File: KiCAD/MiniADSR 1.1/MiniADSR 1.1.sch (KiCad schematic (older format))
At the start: 35 parts, among them J1 INPUT, J2 OUTPUT, J4 ControlBoard_Pins, J6 MainBoard_Pins, Q1 BC547, Q2 BC547, Q3 BC547, U1 LM555xN, U2 TL072

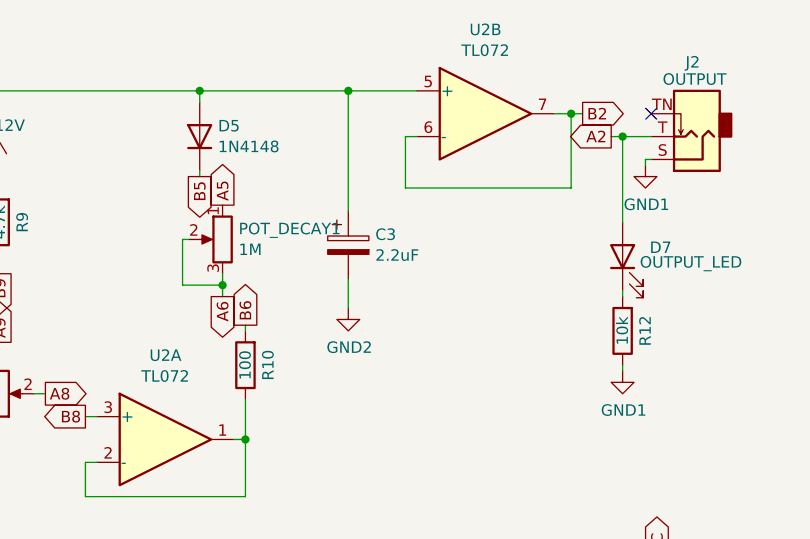
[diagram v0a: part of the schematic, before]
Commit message: increased c3 as recommended by in original design
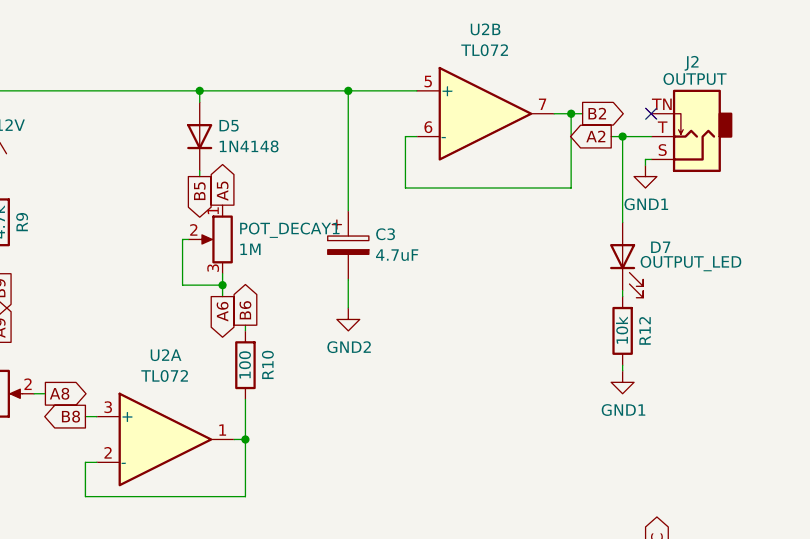
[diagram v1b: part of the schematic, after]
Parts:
- C3: value 2.2uF -> 4.7uF
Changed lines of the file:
@@
 P 9275 2700
 F 0 "C3" H 9393 2746 50  0000 L CNN
-F 1 "2.2uF" H 9393 2655 50  0000 L CNN
+F 1 "4.7uF" H 9393 2655 50  0000 L CNN
 F 2 "Capacitor_THT:CP_Radial_D5.0mm_P2.50mm" H 9313 2550 50  0001 C CNN
 F 3 "~" H 9275 2700 50  0001 C CNN

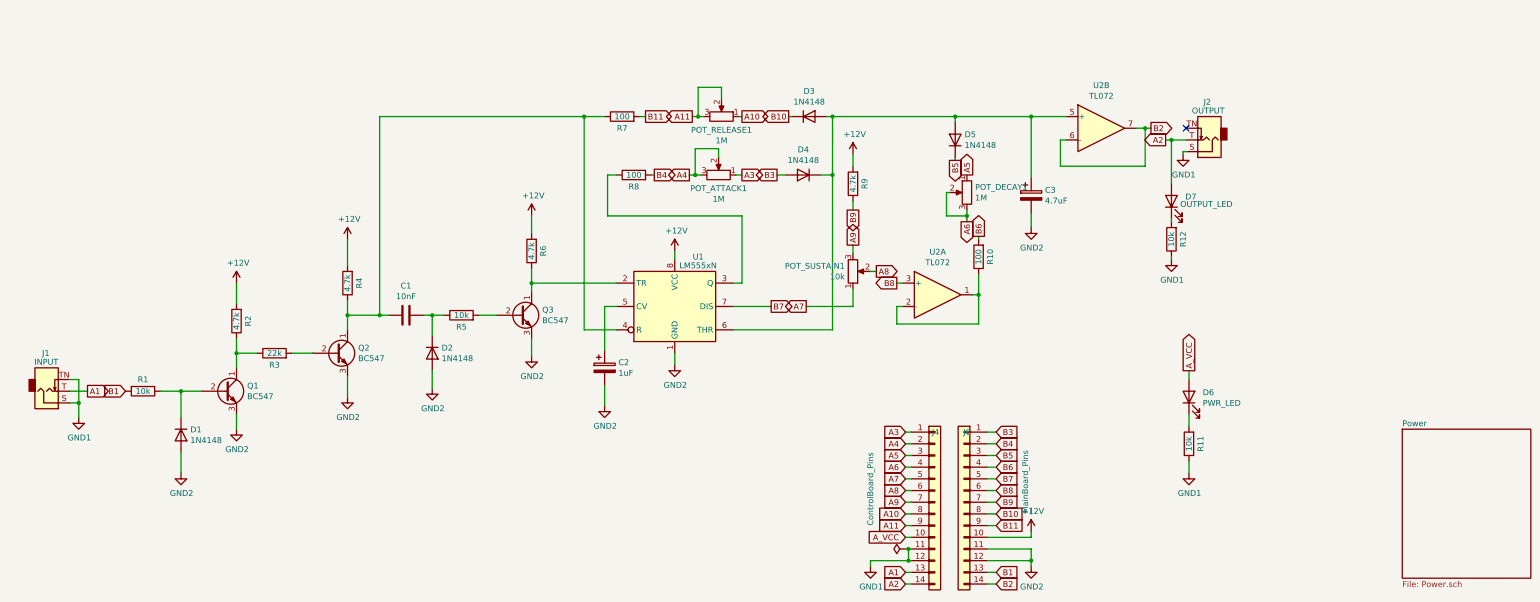
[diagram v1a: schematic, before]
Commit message: Redesigned PCB layout, added cap for longer decay
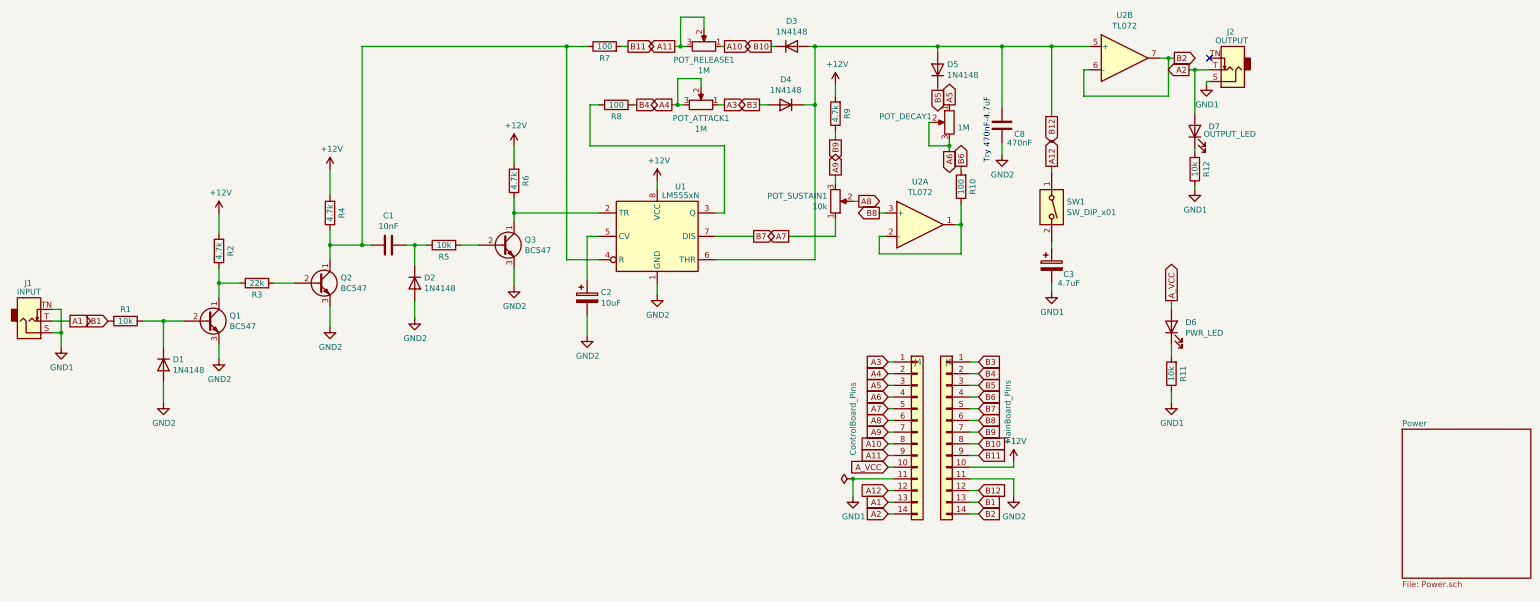
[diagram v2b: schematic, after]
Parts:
- added C8: 470nF, benjiaomodular:Capacitor_Rect_L7.2mm_W2.5mm_P5.00mm, symbol Device:C
- added SW1: SW_DIP_x01, benjiaomodular:ToggleSwitch_MTS-101_SPST, symbol Switch:SW_DIP_x01
- C2: value 1uF -> 10uF
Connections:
- net GND1: now also C3.2; no longer J4.12 (Pin_12)
- net GND2: now also C8.1; no longer C3.2, J6.12 (Pin_12)
- net B12: now reaches D3.2 (A), D4.1 (K), D5.2 (A), U1.6 (THR), U2.5 (+)
- net B12: now also J6.12 (Pin_12), C8.2; no longer C3.1
- new net: C3.1, SW1.2
- new net A12: J4.12 (Pin_12), SW1.1
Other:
- note added: "Try 470nF-4.7uF"
- moved on the sheet: C1, C2, C3, D1, D2, D3, D4, D5, D6, D7, J1, J2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
